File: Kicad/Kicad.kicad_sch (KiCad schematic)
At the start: 4 parts, among them J1 Conn_01x11_Pin, J2 Conn_01x11_Pin, J3 USB_C_Receptacle, J4 USB_C_Receptacle

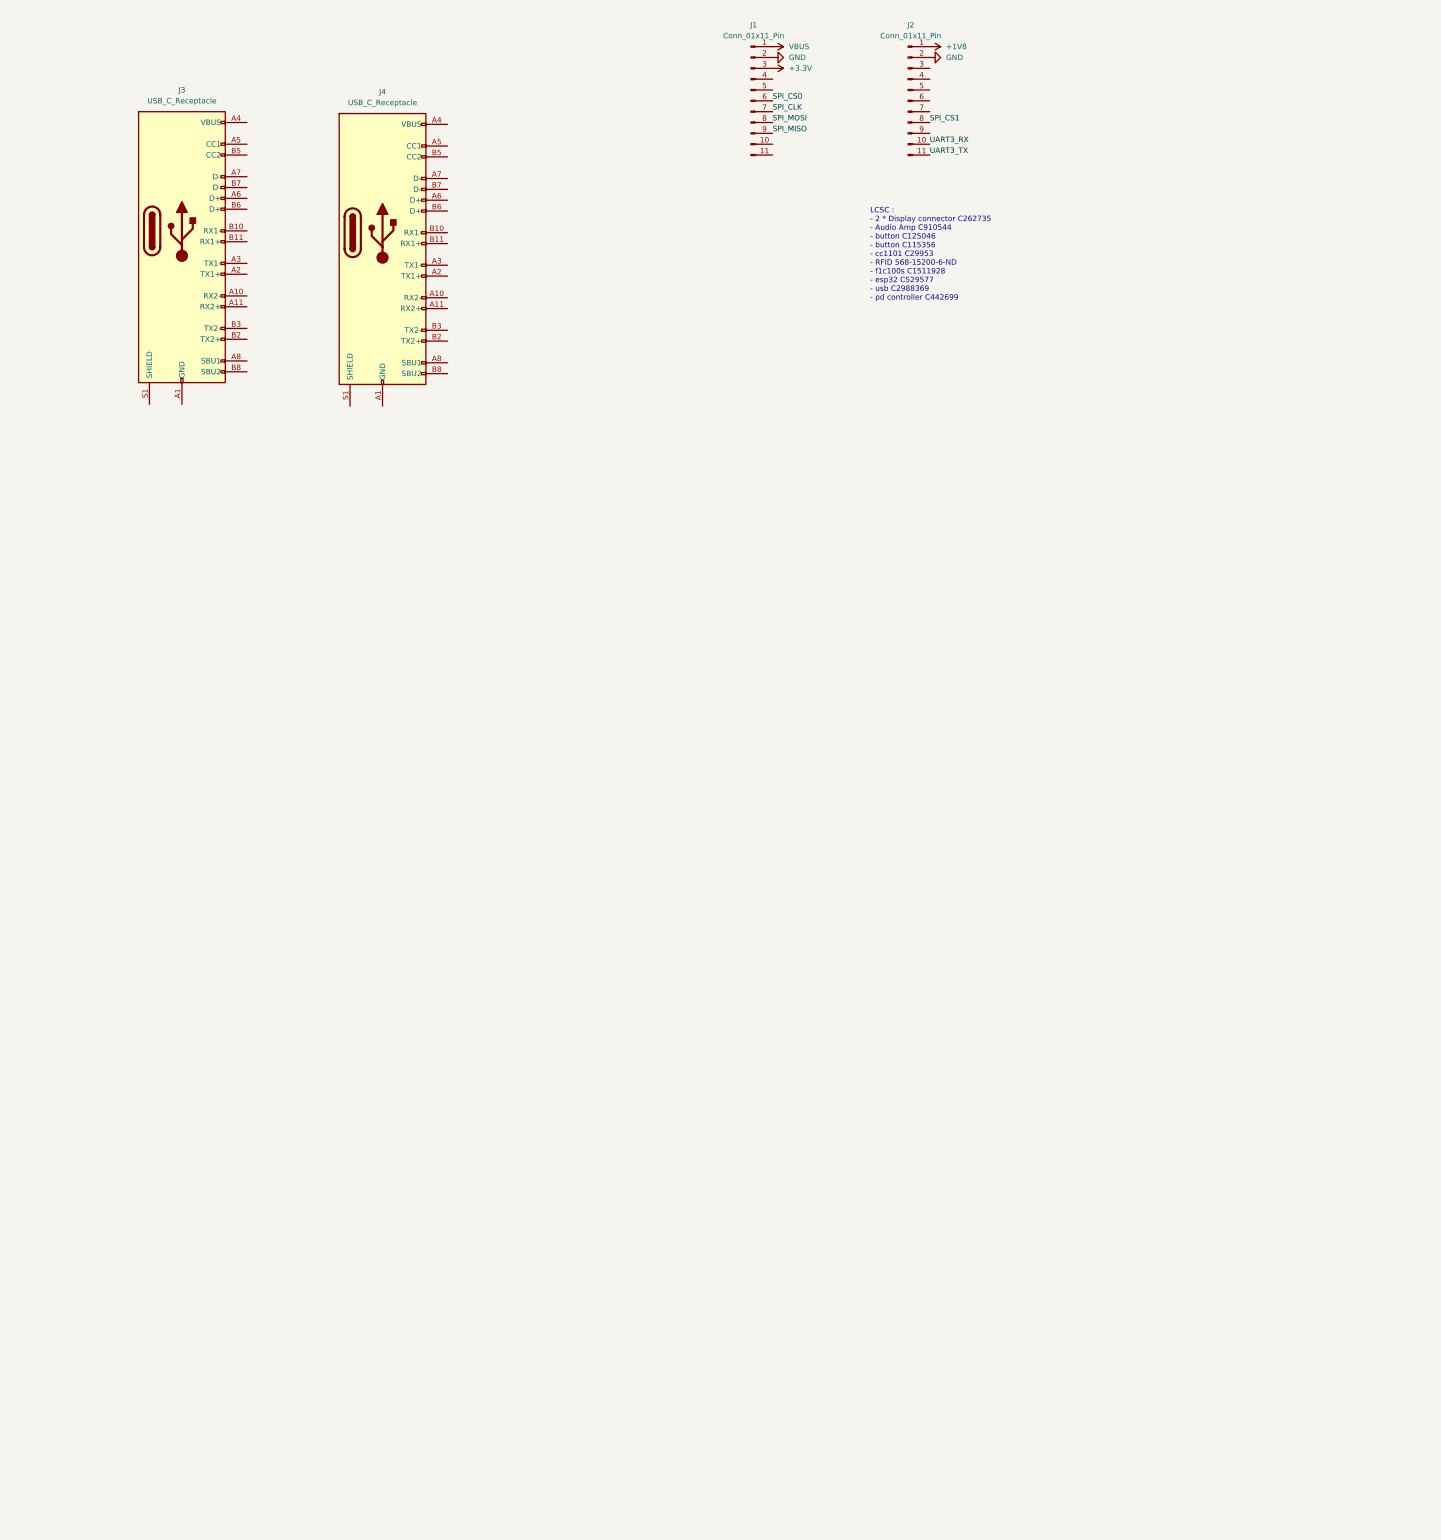
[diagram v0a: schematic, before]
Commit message: add esp32, rv1106, audio chip, buttons, usb and a bunch of cleaning
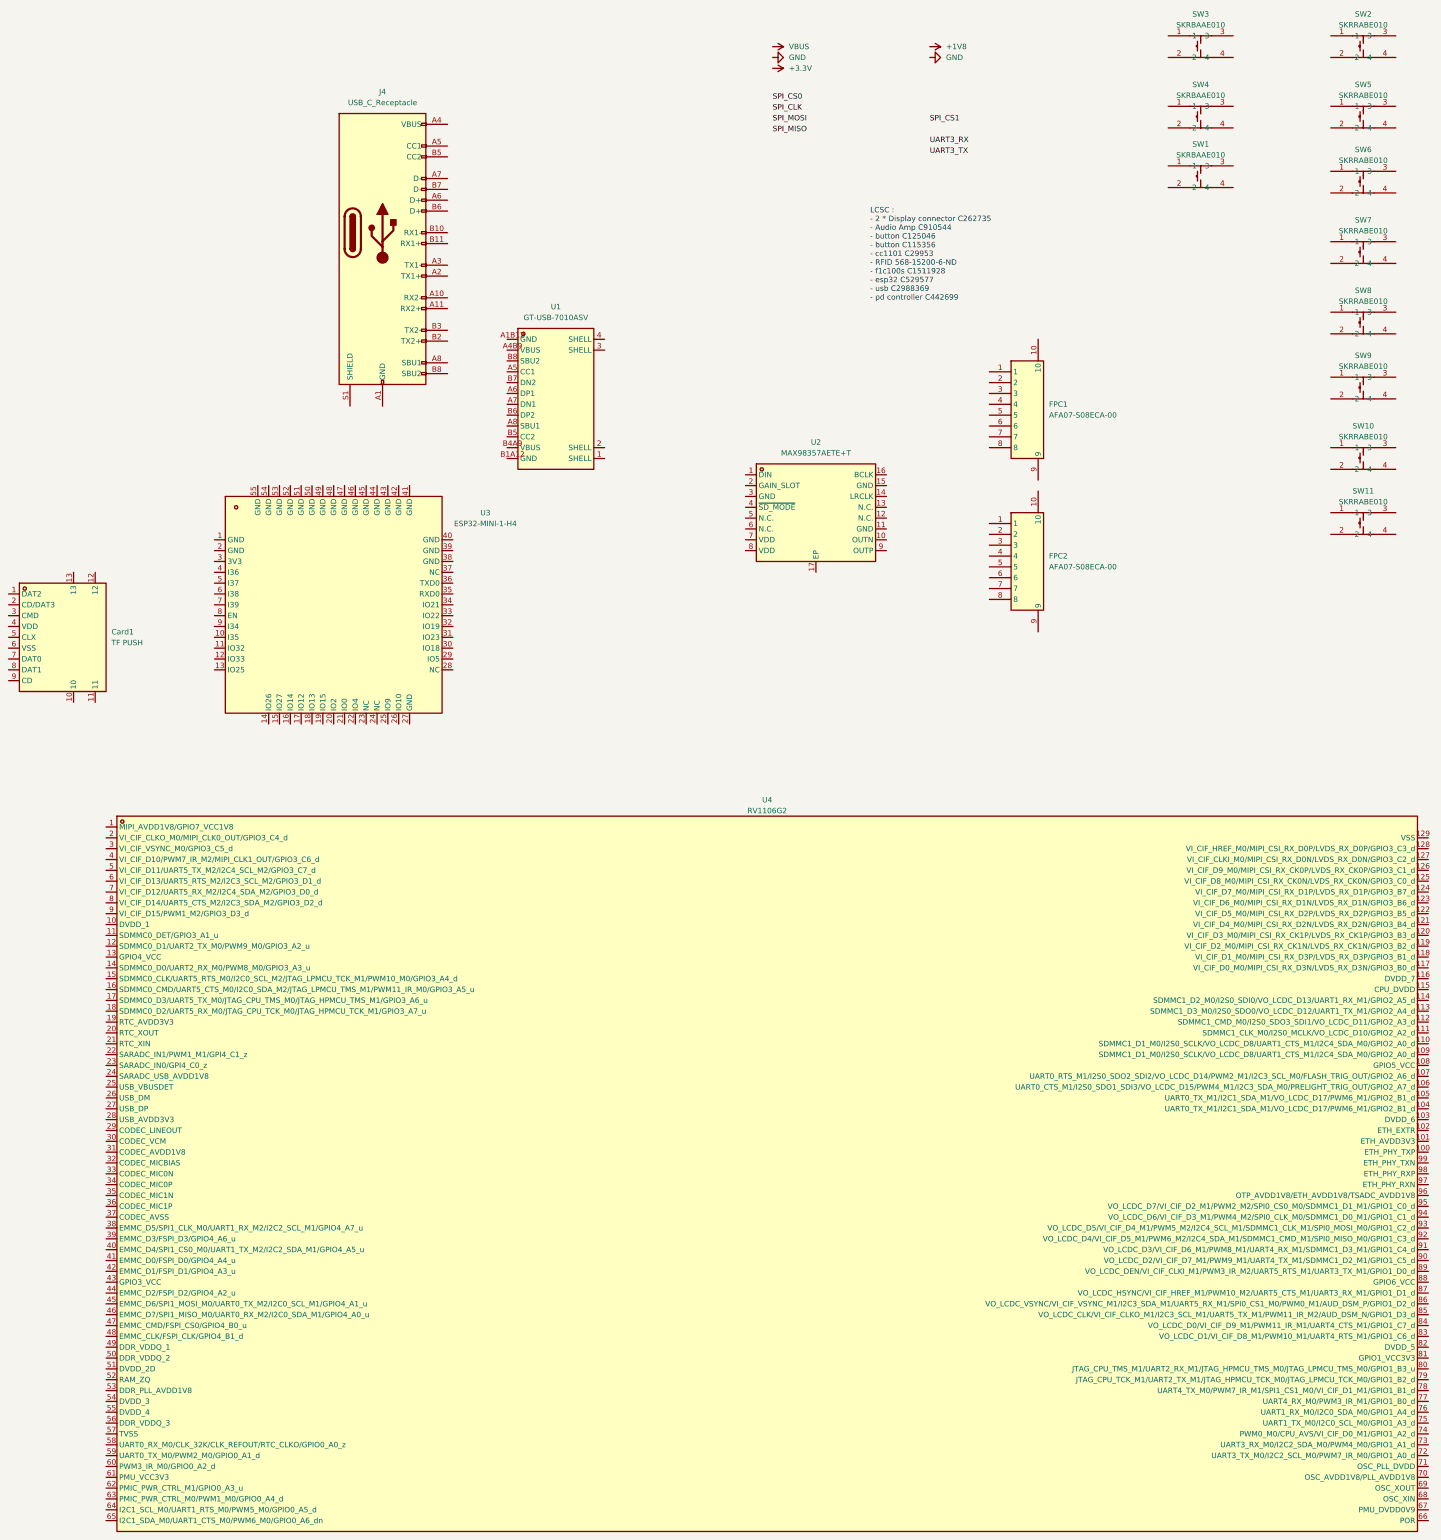
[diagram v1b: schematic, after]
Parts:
- removed J1, J2: Conn_01x11_Pin, Connector_PinSocket_2.54mm:PinSocket_1x11_P2.54mm_Vertical, symbol Connector:Conn_01x11_Pin
- removed J3: USB_C_Receptacle, Connector_USB:USB_C_Receptacle_Amphenol_12401548E4-2A_CircularHoles, symbol Connector:USB_C_Receptacle
- added Card1: TF PUSH, lcsc:TF-SMD_TF-PUSH, symbol lcsc:TFPUSH
- added FPC1, FPC2: AFA07-S08ECA-00, lcsc:FPC-SMD_P1.00-8P_LCS-SJ-H2.5, symbol lcsc:AFA07-S08ECA-00
- added SW1, SW3, SW4: SKRBAAE010, lcsc:KEY-SMD_4P-L4.8-W4.8-P3.65_SKRBAAE010, symbol lcsc:SKRBAAE010
- added SW10, SW11, SW2, SW5, SW6, SW7, SW8, SW9: SKRRABE010, lcsc:KEY-SMD_4P-L7.5-W7.0-P6.00-LS5.0, symbol lcsc:SKRRABE010
- added U1: GT-USB-7010ASV, lcsc:USB-C-SMD_G-SWITCH_GT-USB-7010ASV, symbol lcsc:GT-USB-7010ASV
- added U2: MAX98357AETE+T, lcsc:TQFN-16_L3.0-W3.0-P0.50-BL-EP1.5, symbol lcsc:MAX98357AETE+T
- added U3: ESP32-MINI-1-H4, lcsc:WIFI-SMD_ESP32-MINI-1, symbol lcsc:ESP32-MINI-1-H4
- added U4: RV1106G2, lcsc:QFN-128_L12.3-W12.3-P0.35-TL-EP7.0-1, symbol lcsc:RV1106G2

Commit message: add rv1106 doc, more cleaning
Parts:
- removed J4: USB_C_Receptacle, Connector_USB:USB_C_Receptacle_Amphenol_12401548E4-2A_CircularHoles, symbol Connector:USB_C_Receptacle
- added J1: Conn_01x18, Library:Display18PIN, symbol Connector_Generic:Conn_01x18
- added J2: Conn_01x06, Library:Switch, symbol Connector_Generic:Conn_01x06
- added R1: 10R, Resistor_SMD:R_0805_2012Metric, symbol Device:R
- added R2, R3, R4, R5: 1M, symbol Device:R
- added TP1, TP10, TP11, TP12, TP13, TP14, TP15, TP16, TP2, TP3, TP4, TP5, TP6, TP7, TP8, TP9: TestPoint, TestPoint:TestPoint_Pad_D1.5mm, symbol Connector:TestPoint
- added TP17, TP18: TestPoint, TestPoint:TestPoint_Pad_2.5x2.5mm, symbol Connector:TestPoint
- added U5: GT-USB-7010ASV, lcsc:USB-C-SMD_G-SWITCH_GT-USB-7010ASV, symbol lcsc:GT-USB-7010ASV
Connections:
- net +3.3V: now also FPC1.8, FPC2.1, J1.9 (Pin_9), R1.1, TP8.1, TP9.1
- net GND: now also FPC1.10, FPC1.7, FPC1.9, FPC2.10, FPC2.2, FPC2.9, U2.11 (GND), U2.15 (GND), U2.17 (EP), U3.41 (GND), U3.42 (GND), U3.43 (GND), U3.44 (GND), U3.45 (GND), U3.46 (GND), U3.47 (GND), U3.48 (GND), U3.49 (GND), U3.50 (GND), U3.51 (GND), U3.52 (GND), U3.53 (GND), U3.54 (GND), U3.55 (GND), J2.1 (Pin_1), J2.2 (Pin_2), R2.2, R3.2, R4.2, R5.2, TP10.1, TP7.1
- net MISO: now reaches FPC1.1
- net MISO: now also FPC2.8, J1.7 (Pin_7), TP1.1, TP16.1
- net MOSI: now reaches FPC1.2
- net MOSI: now also FPC2.7, J1.6 (Pin_6), TP15.1, TP2.1
- net C/S: now reaches FPC1.3
- net C/S: now also FPC2.6, J1.5 (Pin_5), TP14.1, TP3.1
- net D/C: now reaches FPC1.4
- net D/C: now also FPC2.5, J1.4 (Pin_4), TP13.1, TP4.1
- net SCK: now reaches FPC1.5
- net SCK: now also FPC2.4, J1.3 (Pin_3), TP12.1, TP5.1
- net RESET: now reaches FPC1.6
- net RESET: now also FPC2.3, J1.2 (Pin_2), TP11.1, TP6.1
- net at U2.10 (OUTN): now also TP17.1
- net at U2.9 (OUTP): now also TP18.1
- net at U1.1 (SHELL): now also U1.2 (SHELL), R3.1
- net at U1.3 (SHELL): now also U1.4 (SHELL), R2.1
- new net: J1.10 (Pin_10), R1.2
- new net: R4.1, U5.3 (SHELL), U5.4 (SHELL)
- new net: J2.4 (Pin_4), J2.5 (Pin_5)
- new net: R5.1, U5.1 (SHELL), U5.2 (SHELL)
- no-connect marks 0 -> 15
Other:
- note added: "Display Breakout"
- note added: "Power Switch"
- note added: "https://fr.aliexpress.com/item/1005003026107533.html?spm=a2g0o.productlist.main.11.23493c60ytg757&algo_pvid=48f93a77-1e04-4e41-b5f6-1a1d738a941e&algo_exp_id=48f93a77-1e04-4e41-b5f6-1a1d738a941e-5&pdp_npi=4%40dis%21EUR%2173.65%2163.82%21%21%2178.54%2168.06%21%402103834817232277456674535ecb73%2112000037263598514%21sea%21FR%21831158873%21X&curPageLogUid=aEg0g27bHKSW&utparam-url=scene%3Asearch%7Cquer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"
- note added: "https://github.com/Gekkio/gb-schematics/tree/main https://wiki.luckfox.com/Luckfox-Pico/Download https://github.com/Gameboypi/SPW/wiki https://github.com/LitchiCheng/RV1106_Linux https://wiki.luckfox.com/Luckfox-Pico/Luckfox-Pico-RV1103/Luckfox-Pico-ResTouch-LCD https://fr.aliexpress.com/item/32632721702.html?spm=a2g0o.productlist.main.11.587bMmZwMmZwu6&algo_pvid=a8e73121-d338-47f6-a910-ee741f30b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"
- moved on the sheet: Card1, FPC1, FPC2, SW1, SW10, SW11, SW2, SW3, SW4, SW5, SW6, SW7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
